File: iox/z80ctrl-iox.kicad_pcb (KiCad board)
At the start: 2 copper layers, 99.8 x 49.9 mm, 22 parts, among them J1 BUS, J10 GPIO_A, J2 BUSEXT, J3 SPI1, J4 SPI2, J5 SPI3, J6 SPI4, J7 GPIO_A, J8 GPIO_A, J9 GPIO_A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

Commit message: Add RTC
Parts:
- added BT1: Battery_Cell, Battery:BatteryHolder_Keystone_3001_1x12mm, F.Cu at (171.0, 118.9)
- added C4: .1uf, Capacitor_THT:C_Disc_D4.7mm_W2.5mm_P5.00mm, F.Cu at (202.4, 109.7)
- added U4: DS1306+, Package_DIP:DIP-16_W7.62mm_Socket, F.Cu at (205.7, 117.3)
- added Y1: Crystal_Small, Crystal:Crystal_DS26_D2.0mm_L6.0mm_Horizontal, F.Cu at (228.5, 115.1)
- J3, J4, J5, J6: footprint Connector_PinHeader_2.54mm:PinHeader_2x03_P2.54mm_Horizontal -> Connector_PinHeader_2.54mm:PinHeader_1x06_P2.54mm_Horizontal
- J7: value GPIO_A -> GPIO_B
- J8: value GPIO_A -> GPIO_C
- J9: value GPIO_A -> GPIO_D
- U1: footprint Package_DIP:DIP-14_W7.62mm -> Package_DIP:DIP-14_W7.62mm_Socket
- U2, U3: footprint Package_DIP:DIP-28_W7.62mm -> Package_DIP:DIP-28_W7.62mm_Socket
- moved J6 42.2 mm to (171.3, 104.8)
- moved J5 31.2 mm to (192.4, 104.8)
- moved J4 20.2 mm to (213.6, 104.8)
- moved J3 9.45 mm to (234.7, 104.8)
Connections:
- J2 pad 22: (no net) -> /~AUXCS1~
- J3 pad 1: /SCK -> /~EXTCS1~
- J3 pad 2: VCC -> /MOSI
- J3 pad 3: /MOSI -> /MISO
- J3 pad 4: /~EXTCS1~ -> /SCK
- J3 pad 5: /MISO -> GND
- J3 pad 6: GND -> VCC
- J4 pad 1: /SCK -> /~EXTCS2~
- J4 pad 2: VCC -> /MOSI
- J4 pad 3: /MOSI -> /MISO
- J4 pad 4: /~EXTCS2~ -> /SCK
- J4 pad 5: /MISO -> GND
- J4 pad 6: GND -> VCC
- J5 pad 1: /SCK -> /~EXTCS3~
- J5 pad 2: VCC -> /MOSI
- J5 pad 3: /MOSI -> /MISO
- J5 pad 4: /~EXTCS3~ -> /SCK
- J5 pad 5: /MISO -> GND
- J5 pad 6: GND -> VCC
- J6 pad 1: /SCK -> /~EXTCS4~
- J6 pad 2: VCC -> /MOSI
- J6 pad 3: /MOSI -> /MISO
- J6 pad 4: /~EXTCS4~ -> /SCK
- J6 pad 5: /MISO -> GND
- J6 pad 6: GND -> VCC
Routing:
- net /~AUXCS1~: track 0.00 -> 59.3 mm, vias 0 -> 2
- net Net-(BT1-Pad1): track 0.00 -> 54.2 mm, vias 0 -> 1
- net VCC: track 296.8 -> 344.5 mm
- net /SCK: track 140.8 -> 182.1 mm, vias 1 -> 4
- net /MISO: track 148.0 -> 186.6 mm, vias 1 -> 4
- net /MOSI: track 142.5 -> 177.8 mm, vias 6 -> 4
- net /~EXTCS4~: track 16.6 -> 51.2 mm, vias 1 -> 0
- net /~EXTCS3~: track 16.6 -> 40.3 mm
- net Net-(U4-Pad3): track 0.00 -> 19.5 mm
- net Net-(U4-Pad4): track 0.00 -> 16.1 mm
- net /~EXTCS2~: track 29.5 -> 41.1 mm
- net /~EXTCS1~: track 46.3 -> 42.6 mm
- net /GPB0: track 45.5 -> 44.9 mm
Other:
- board text added: "z80ctrl IO expander REV1 (C)2018 J.B. Langston https://github.com/jblang/z80ctrl"
- board text removed: "z80ctrl REV3 (C)2018 J.B. Langston https://github.com/jblang/z80ctrl"

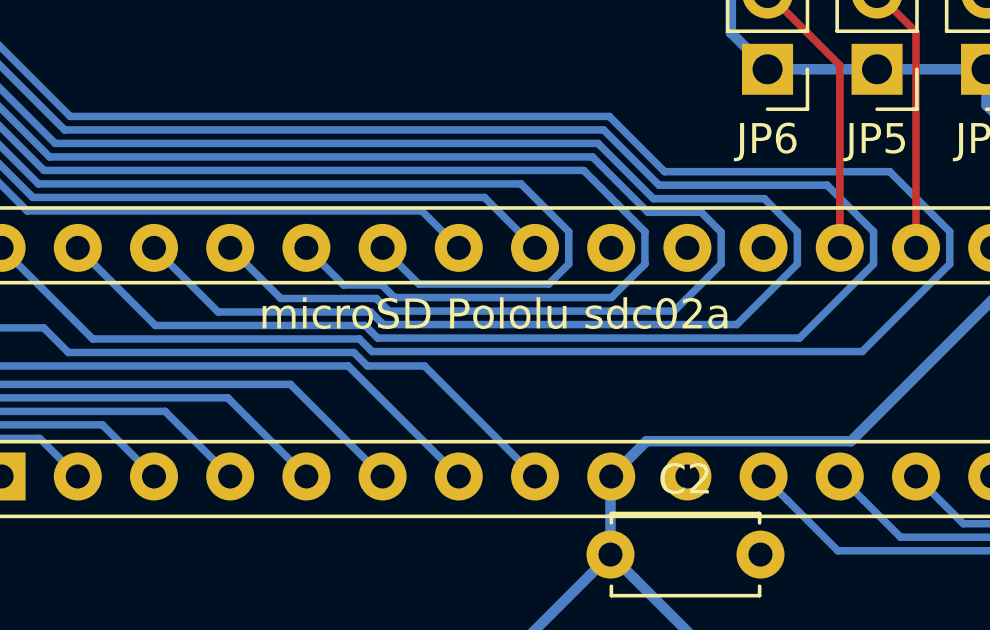
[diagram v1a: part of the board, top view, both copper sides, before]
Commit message: Remove extra text from IOX module
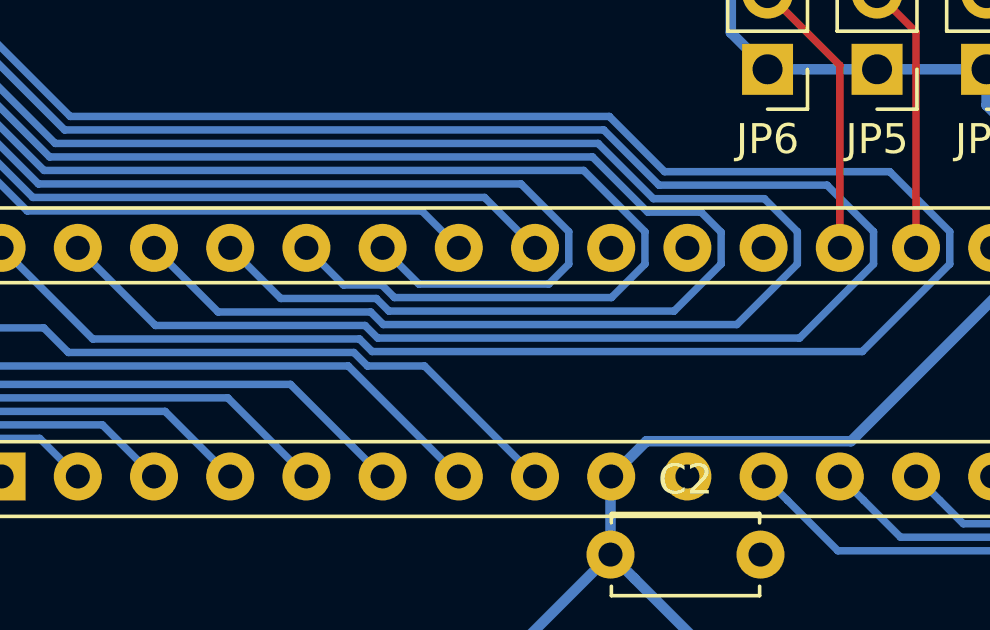
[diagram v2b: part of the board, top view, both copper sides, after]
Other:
- board text removed: "microSD Pololu sdc02a"
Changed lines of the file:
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@@
   (general
     (thickness 1.6)
-    (drawings 14)
+    (drawings 13)
     (tracks 666)
     (zones 0)
@@
   (gr_line (start 155.32608 143.01978) (end 156.8958 143.01978) (angle 90) (layer F.SilkS) (width 0.2))
   (gr_line (start 169.164 103.505) (end 154.1526 118.5164) (angle 90) (layer Edge.Cuts) (width 0.15))
-  (gr_text "microSD Pololu sdc02a" (at 182.3085 136.0805) (layer F.SilkS)
-    (effects (font (size 1 1) (thickness 0.15)))
-  )
   (gr_line (start 156.8958 143.01978) (end 156.8958 153.13152) (angle 90) (layer F.SilkS) (width 0.2))
   (gr_line (start 154.14498 153.13152) (end 154.14498 144.20088) (angle 90) (layer F.SilkS) (width 0.2))

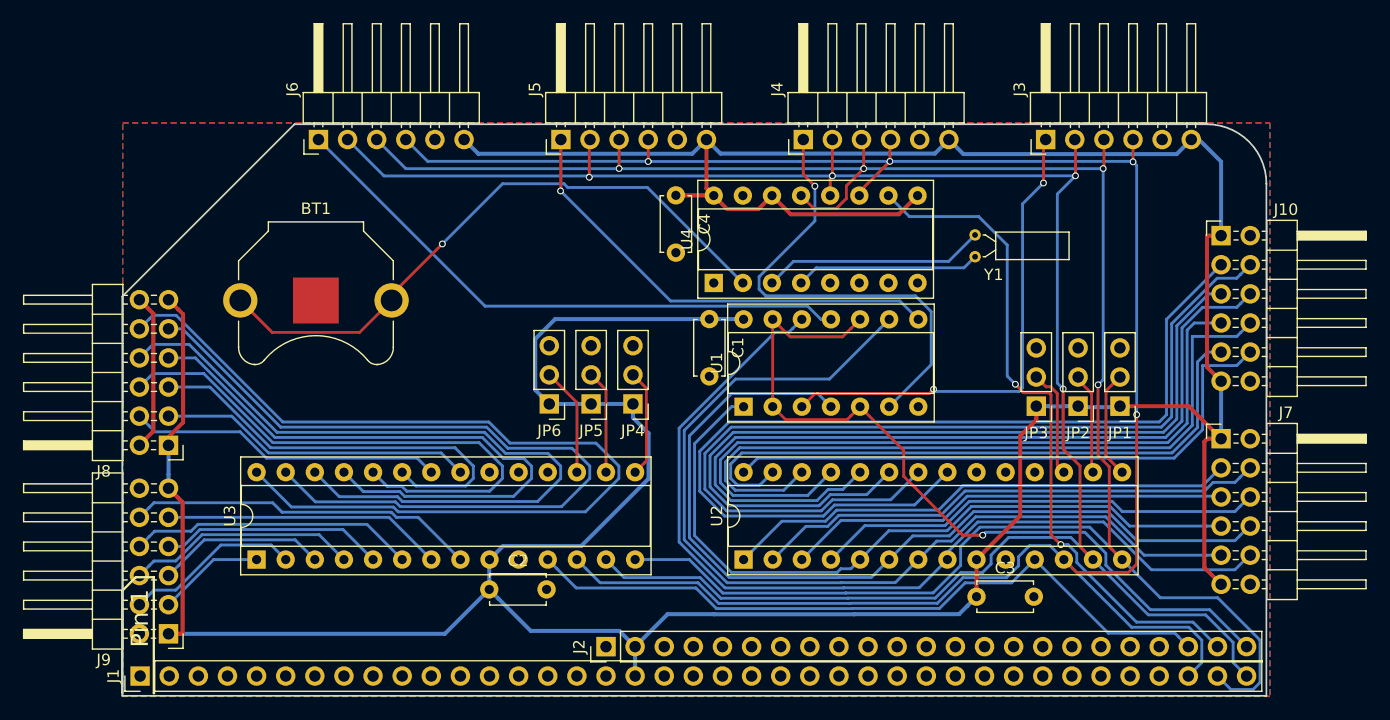
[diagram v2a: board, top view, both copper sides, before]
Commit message: Final tweaks to I/O expander
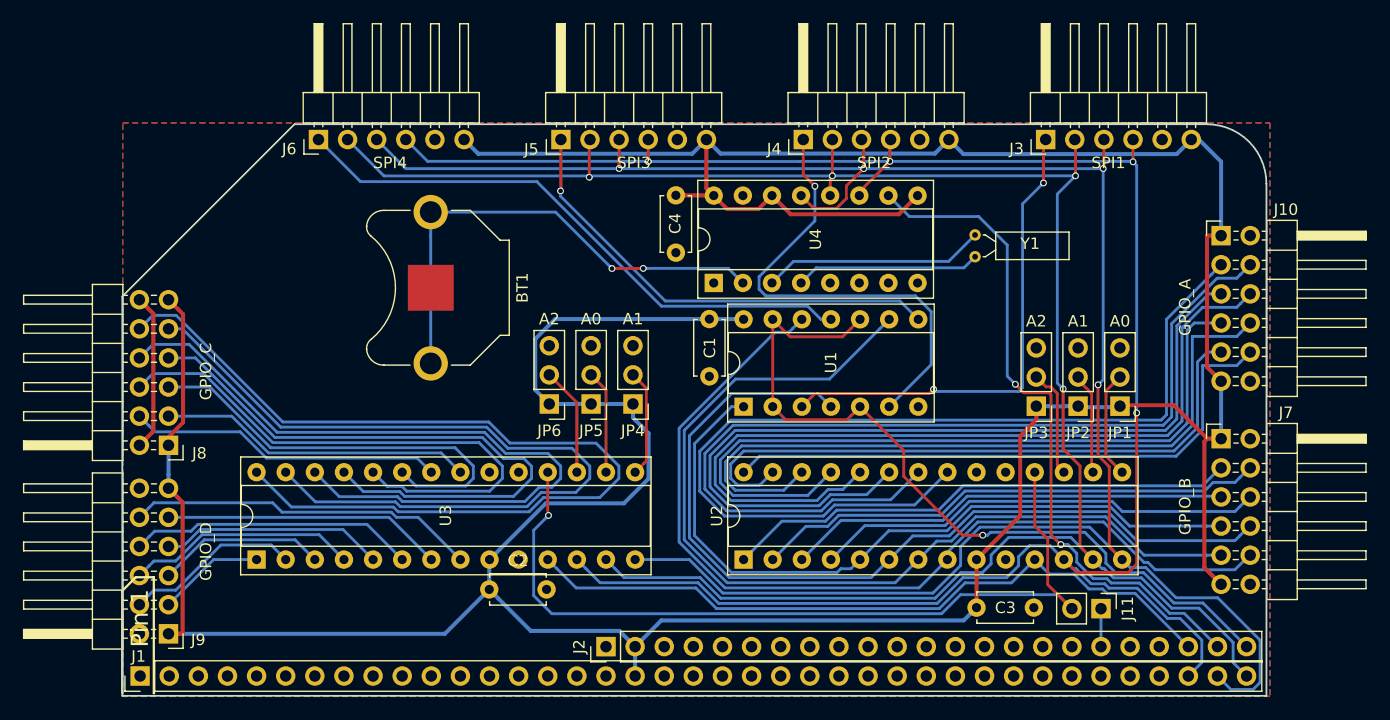
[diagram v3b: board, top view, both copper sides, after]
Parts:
- added J11: Conn_01x02, Connector_PinHeader_2.54mm:PinHeader_1x02_P2.54mm_Vertical, F.Cu at (239.5, 145.8)
- moved BT1 10.1 mm to (181.1, 117.8), turned to 270 degrees
- moved C3 0.95 mm to (228.7, 145.7)
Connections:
- J2 pad 18: (no net) -> Net-(J11-Pad1)
- U2 pad 18: (no net) -> /~AVRRST~
- U3 pad 18: (no net) -> /~AVRRST~
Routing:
- net /~AVRRST~: track 0.00 -> 73.4 mm, vias 0 -> 1
- net Net-(BT1-Pad1): track 54.2 -> 43.0 mm, vias 1 -> 2
- net Net-(J11-Pad1): track 0.00 -> 3.32 mm
- net VCC: track 344.5 -> 343.9 mm

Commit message: Prepare for REV2 of IOX board
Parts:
- added C5: .1uf, Capacitor_THT:C_Disc_D4.7mm_W2.5mm_P5.00mm, F.Cu at (186.8, 110.2)
- added U5: 74HCT04, Package_DIP:DIP-14_W7.62mm_Socket, F.Cu at (190.2, 117.8)
- BT1: value Battery_Cell -> CR1216
- J11: value Conn_01x02 -> RESET; footprint Connector_PinHeader_2.54mm:PinHeader_1x02_P2.54mm_Vertical -> Connector_PinHeader_2.54mm:PinHeader_1x03_P2.54mm_Vertical
- J3, J4, J5, J6: footprint Connector_PinHeader_2.54mm:PinHeader_1x06_P2.54mm_Horizontal -> Connector_PinHeader_2.54mm:PinHeader_1x07_P2.54mm_Horizontal
- Y1: value Crystal_Small -> 32kHz
- moved C1 41.7 mm to (164.9, 110.1)
- moved U1 41.4 mm to (168.2, 117.8)
- moved BT1 34.8 mm to (215.1, 124.8), turned to 180 degrees
- moved U4 22.1 mm to (227.9, 117.9)
- moved C4 21.9 mm to (224.3, 110.3)
- moved Y1 7.05 mm to (227.4, 122.0), turned to 0 degrees
- moved J11 2.59 mm to (242.1, 145.7)
- moved J3 0.89 mm to (233.8, 104.8)
- moved J4 0.81 mm to (212.7, 104.8)
- moved J5 0.73 mm to (191.7, 104.8)
- moved J6 0.65 mm to (170.6, 104.8)
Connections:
- J3 pad 1: /~EXTCS1~ -> /EXTCS1
- J3 pad 2: /MOSI -> /~EXTCS1~
- J3 pad 3: /MISO -> /MOSI
- J3 pad 4: /SCK -> /MISO
- J3 pad 5: GND -> /SCK
- J3 pad 6: VCC -> GND
- J4 pad 1: /~EXTCS2~ -> /EXTCS2
- J4 pad 2: /MOSI -> /~EXTCS2~
- J4 pad 3: /MISO -> /MOSI
- J4 pad 4: /SCK -> /MISO
- J4 pad 5: GND -> /SCK
- J4 pad 6: VCC -> GND
- J5 pad 1: /~EXTCS3~ -> /EXTCS3
- J5 pad 2: /MOSI -> /~EXTCS3~
- J5 pad 3: /MISO -> /MOSI
- J5 pad 4: /SCK -> /MISO
- J5 pad 5: GND -> /SCK
- J5 pad 6: VCC -> GND
- J6 pad 1: /~EXTCS4~ -> /EXTCS4
- J6 pad 2: /MOSI -> /~EXTCS4~
- J6 pad 3: /MISO -> /MOSI
- J6 pad 4: /SCK -> /MISO
- J6 pad 5: GND -> /SCK
- J6 pad 6: VCC -> GND
- U1 pad 1: /GPB4 -> /GPB7
- U1 pad 11: /~EXTCS4~ -> /~EXTCS3~
- U1 pad 12: /GPB7 -> /GPB6
- U1 pad 3: /~EXTCS1~ -> /~EXTCS4~
- U1 pad 8: /~EXTCS3~ -> /~EXTCS1~
- U1 pad 9: /GPB6 -> /GPB4
- U4 pad 10: /~AUXCS1~ -> /AUXCS1
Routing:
- net /~AUXCS2~: track 69.5 -> 125.9 mm
- net /EXTCS1: track 0.00 -> 48.9 mm, vias 0 -> 1
- net /AUXCS1: track 0.00 -> 45.2 mm
- net /EXTCS4: track 0.00 -> 32.6 mm
- net /GPB4: track 63.9 -> 95.3 mm
- net /EXTCS2: track 0.00 -> 23.8 mm, vias 0 -> 1
- net /GPB7: track 81.0 -> 104.8 mm
- net /GPB6: track 83.5 -> 105.0 mm
- net /~EXTCS1~: track 42.6 -> 63.3 mm, vias 2 -> 1
- net /~AUXCS1~: track 59.3 -> 79.0 mm, vias 2 -> 1
- net Net-(BT1-Pad1): track 43.0 -> 24.7 mm, vias 2 -> 0
- net /GPB5: track 77.5 -> 95.5 mm
- net /EXTCS3: track 0.00 -> 17.6 mm, vias 0 -> 1
- net Net-(U4-Pad3): track 19.5 -> 5.58 mm
- net /~EXTCS4~: track 51.2 -> 41.6 mm
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
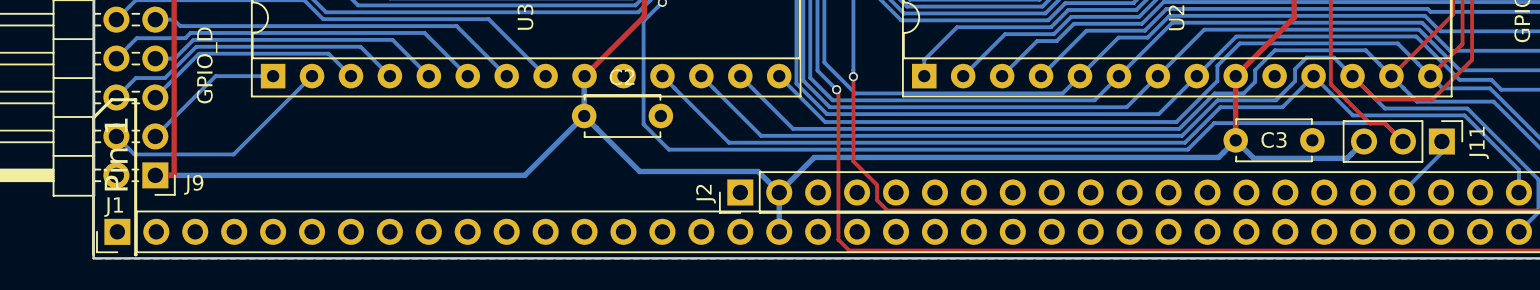
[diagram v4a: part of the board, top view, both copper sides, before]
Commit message: Update silkscreen for REV2
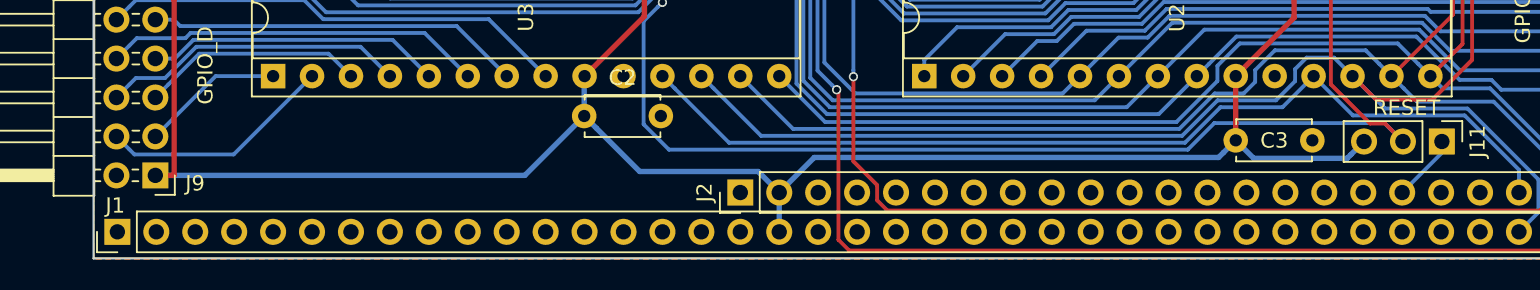
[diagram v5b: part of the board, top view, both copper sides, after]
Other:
- board text added: "z80ctrl IO expander REV2 (C)2018 J.B. Langston https://github.com/jblang/z80ctrl"
- board text removed: "Pin 1"
- board text removed: "z80ctrl IO expander REV1 (C)2018 J.B. Langston https://github.com/jblang/z80ctrl"
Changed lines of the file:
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@@
   (general
     (thickness 1.6)
-    (drawings 13)
+    (drawings 7)
     (tracks 733)
     (zones 0)
@@
       (effects (font (size 1 1) (thickness 0.15)))
     )
-    (fp_text value RESET (at 0 7.41 270) (layer F.Fab)
+    (fp_text value RESET (at -2.1971 2.2987) (layer F.SilkS)
       (effects (font (size 1 1) (thickness 0.15)))
     )
@@
     )
   )
-  (gr_text "z80ctrl IO expander REV1\n(C)2018 J.B. Langston\nhttps://github.com/jblang/z80ctrl" (at 180.8607 117.6147) (layer B.SilkS)
-    (effects (font (size 1.5 1.5) (thickness 0.3)) (justify mirror))
-  )
-  (gr_line (start 154.14498 144.20088) (end 155.32608 143.01978) (angle 90) (layer F.SilkS) (width 0.2))
+  (gr_text "z80ctrl IO expander REV2\n(C)2018 J.B. Langston\nhttps://github.com/jblang/z80ctrl" (at 174.879 126.3904) (layer B.SilkS)
+    (effects (font (size 1.1 1.1) (thickness 0.2)) (justify mirror))
+  )
   (gr_arc (start 248.7706 108.685) (end 248.7708 103.505) (angle 90) (layer Edge.Cuts) (width 0.15))
   (gr_line (start 248.7708 103.505) (end 169.164 103.505) (angle 90) (layer Edge.Cuts) (width 0.15))
-  (gr_line (start 155.32608 143.01978) (end 156.8958 143.01978) (angle 90) (layer F.SilkS) (width 0.2))
   (gr_line (start 169.164 103.505) (end 154.1526 118.5164) (angle 90) (layer Edge.Cuts) (width 0.15))
-  (gr_line (start 156.8958 143.01978) (end 156.8958 153.13152) (angle 90) (layer F.SilkS) (width 0.2))
-  (gr_line (start 154.14498 153.13152) (end 154.14498 144.20088) (angle 90) (layer F.SilkS) (width 0.2))
-  (gr_text "Pin 1" (at 155.68168 146.60118 90) (layer F.SilkS)
-    (effects (font (size 1.5 1.5) (thickness 0.3)))
-  )
-  (gr_line (start 156.8958 153.13152) (end 156.93136 153.13152) (angle 90) (layer F.SilkS) (width 0.2))
   (gr_line (start 253.9526 108.685) (end 253.9526 153.3652) (angle 90) (layer Edge.Cuts) (width 0.15))
   (gr_line (start 154.1526 118.5164) (end 154.1526 153.3652) (angle 90) (layer Edge.Cuts) (width 0.15))

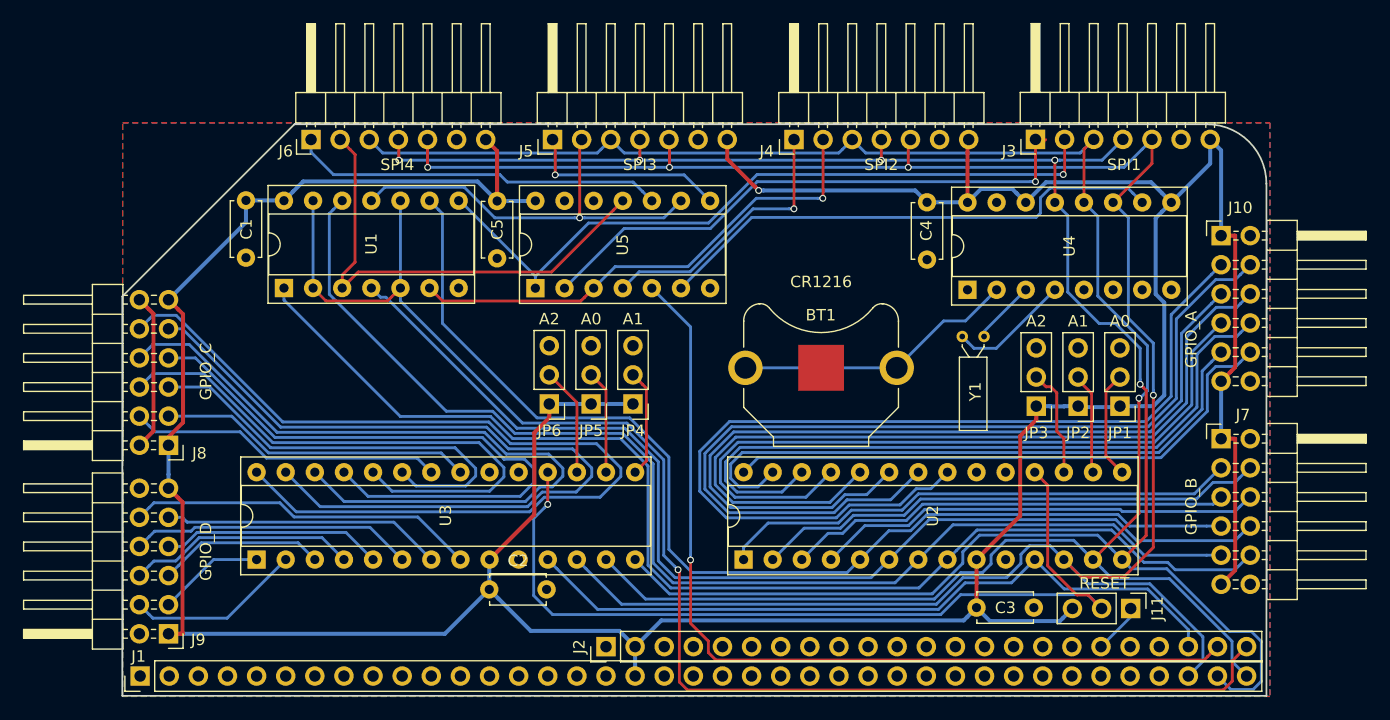
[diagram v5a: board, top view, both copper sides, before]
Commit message: Switch to same capacitor footprint as z80ctrl board
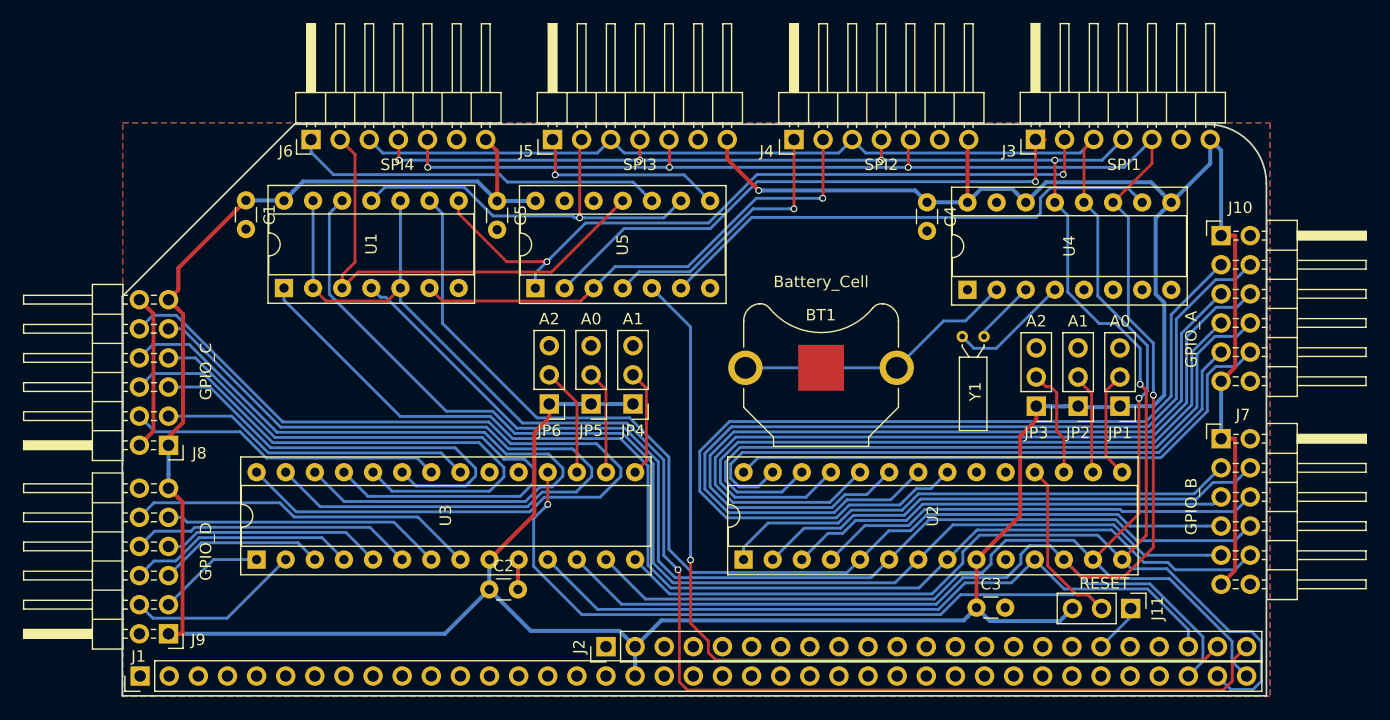
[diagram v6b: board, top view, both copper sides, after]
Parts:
- BT1: value CR1216 -> Battery_Cell
- C1, C2, C3, C4, C5: footprint Capacitor_THT:C_Disc_D4.7mm_W2.5mm_P5.00mm -> Capacitor_THT:C_Disc_D3.0mm_W1.6mm_P2.50mm
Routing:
- net GND: track 13.7 -> 16.3 mm
- net /~AVRRST~: track 77.6 -> 76.1 mm
- net /~EXTCS1~: track 63.3 -> 64.6 mm, vias 1 -> 2
